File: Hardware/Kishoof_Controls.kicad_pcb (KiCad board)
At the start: 4 copper layers, 70.8 x 110 mm, 30 parts, among them J1 Conn_01x12_Pin, J10 Audio_Out_L, J11 Audio_Out_R, J12 USB_C_Receptacle, J14 Conn_01x01_Socket, J2 Conn_01x12_Pin, J3 Conn_01x12_Pin, J4 Conn_01x12_Pin, J5 WavetablePosA, J6 WavetablePosB, J7 WarpCV, J8 VOct, J9 VCA, SW1 SW_Push, SW2 Mode_Switch, SW3 Octave_Switch, SW4 ChB_Output, SW5 Encoder, U1 STF202-22T1G

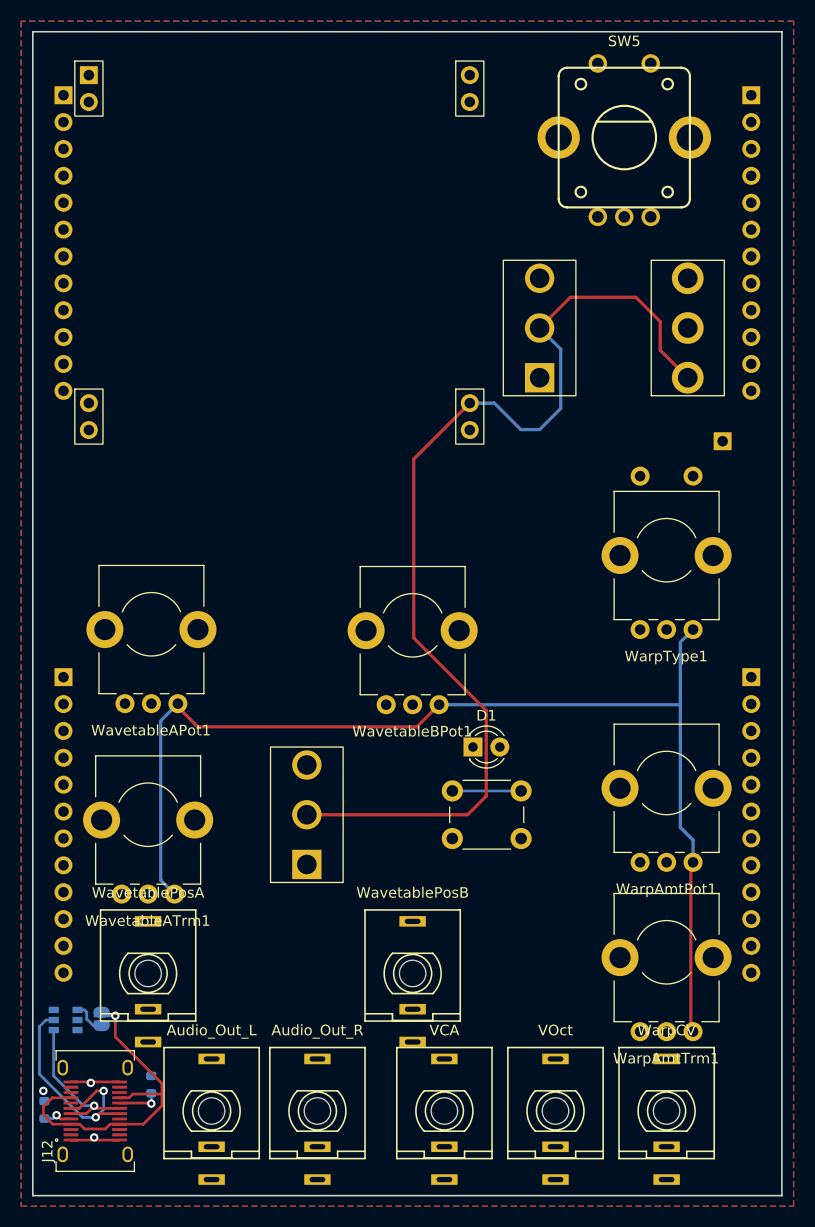
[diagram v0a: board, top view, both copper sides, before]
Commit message: Control board routed; updated lcd riser
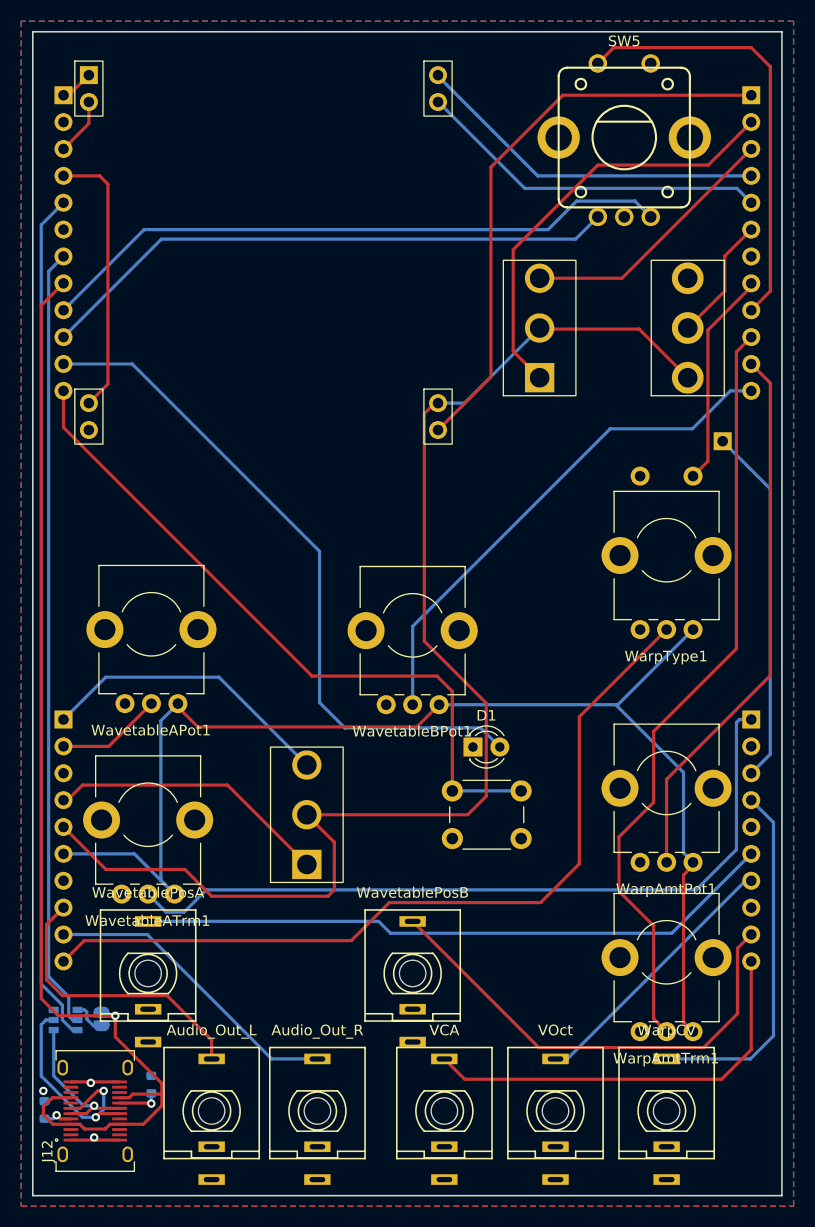
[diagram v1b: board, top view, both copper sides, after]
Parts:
- J3, J4: value Conn_01x12_Pin -> Conn_01x10_Pin; footprint Connector_PinSocket_2.54mm:PinSocket_1x12_P2.54mm_Vertical -> Connector_PinSocket_2.54mm:PinSocket_1x10_P2.54mm_Vertical
- moved J3 4.00 mm to (58.0, 104.0)
- moved J4 4.00 mm to (123.0, 104.0)
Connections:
- J1 pad 1: /LCD_SPI3_SS -> /LCD_SPI3_MOSI
- J1 pad 10: USB_VBUS -> /Encoder_Up
- J1 pad 11: /B_Octave_Btn -> /LED_Oct_B_Out
- J1 pad 12: unconnected-(J1-Pin_12-Pad12) -> /B_Octave_Btn
- J1 pad 2: /LCD_DC -> GND
- J1 pad 3: /Octave_Up -> /LCD_SPI3_SCK
- J1 pad 4: /Octave_Down -> /LCD_SPI3_SS
- J1 pad 5: unconnected-(J1-Pin_5-Pad5) -> /USB_DP
- J1 pad 6: /LCD_SPI3_MOSI -> GND
- J1 pad 7: /LCD_SPI3_SCK -> /USB_DM
- J1 pad 8: /USB_DM -> USB_VBUS
- J1 pad 9: /USB_DP -> /Encoder_Down
- J2 pad 1: unconnected-(J2-Pin_1-Pad1) -> /LCD_Backlight
- J2 pad 10: /Warp_Type_Pot -> /Warp_Amt_Trm
- J2 pad 11: /Audio_Out_R -> /Warp_Amt_Pot
- J2 pad 12: /Audio_Out_L -> /Wavetable_Pos_B_Pot
- J2 pad 2: /ChB_RM -> /Octave_Up
- J2 pad 3: /Wavetable_Pos_A_Pot -> /Octave_Down
- J2 pad 4: /Wavetable_Pos_B_CV_In -> /LCD_DC
- J2 pad 5: +3.3V -> /LCD_RESET
- J2 pad 6: GND -> Mode
- J2 pad 7: +3.3VA -> GND
- J2 pad 8: /Warp_Amt_Trm -> /Warp_Polarity_Btn
- J2 pad 9: /Warp_Amt_Pot -> /Encoder_Btn
- J3 pad 1: /LCD_RESET -> /ChB_RM
- J3 pad 10: unconnected-(J3-Pin_10-Pad10) -> /Warp_Type_Pot
- J3 pad 2: /Warp_Polarity_Btn -> /Wavetable_Pos_A_Pot
- J3 pad 3: /Encoder_Up -> GND
- J3 pad 4: /Encoder_Down -> /ChB_Mix
- J3 pad 5: /Wavetable_Pos_B_Pot -> +3.3V
- J3 pad 6: unconnected-(J3-Pin_6-Pad6) -> +3.3VA
- J3 pad 7: unconnected-(J3-Pin_7-Pad7) -> GND
- J3 pad 8: Mode -> /Audio_Out_L
- J3 pad 9: unconnected-(J3-Pin_9-Pad9) -> /Audio_Out_R
- J4 pad 1: unconnected-(J4-Pin_1-Pad1) -> /Wavetable_Pos_A_Trm
- J4 pad 10: unconnected-(J4-Pin_10-Pad10) -> /VCA_CV_In
- J4 pad 2: /LED_Oct_B_Out -> GND
- J4 pad 3: /LCD_Backlight -> /Ext_Audio_In
- J4 pad 4: /Wavetable_Pos_A_Trm -> /Warp_CV_In
- J4 pad 5: unconnected-(J4-Pin_5-Pad5) -> GND
- J4 pad 6: /ChB_Mix -> /Wavetable_Pos_A_CV_In
- J4 pad 7: unconnected-(J4-Pin_7-Pad7) -> /Pitch_CV_In
- J4 pad 8: /Encoder_Btn -> GND
- J4 pad 9: /VCA_CV_In -> /Wavetable_Pos_B_CV_In
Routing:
- net /USB_DP: track 0.00 -> 80.8 mm
- net /Warp_Type_Pot: track 0.00 -> 78.1 mm
- net USB_VBUS: track 32.3 -> 108.4 mm
- net /USB_DM: track 0.00 -> 74.1 mm
- net /Warp_Amt_Trm: track 0.00 -> 72.7 mm
- net /Wavetable_Pos_A_Trm: track 0.00 -> 72.3 mm
- net /LED_Oct_B_Out: track 0.00 -> 64.6 mm
- net /Wavetable_Pos_A_CV_In: track 0.00 -> 60.6 mm
- net /Encoder_Down: track 0.00 -> 60.4 mm
- net /B_Octave_Btn: track 6.50 -> 66.4 mm
- net /Encoder_Up: track 0.00 -> 55.2 mm
- net /LCD_Backlight: track 0.00 -> 54.3 mm
- net /Warp_Amt_Pot: track 0.00 -> 51.9 mm
- net /Wavetable_Pos_B_Pot: track 0.00 -> 48.6 mm
- net /Wavetable_Pos_B_CV_In: track 0.00 -> 45.0 mm
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- removed copper zone on In2.Cu, net (none)
- removed copper zone on In1.Cu, net GND
- removed copper zone on In2.Cu, net GND
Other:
- copper layers 4 -> 2
- board text removed: "RX"
- board text removed: "TX"

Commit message: PCBs v1.0 ordered
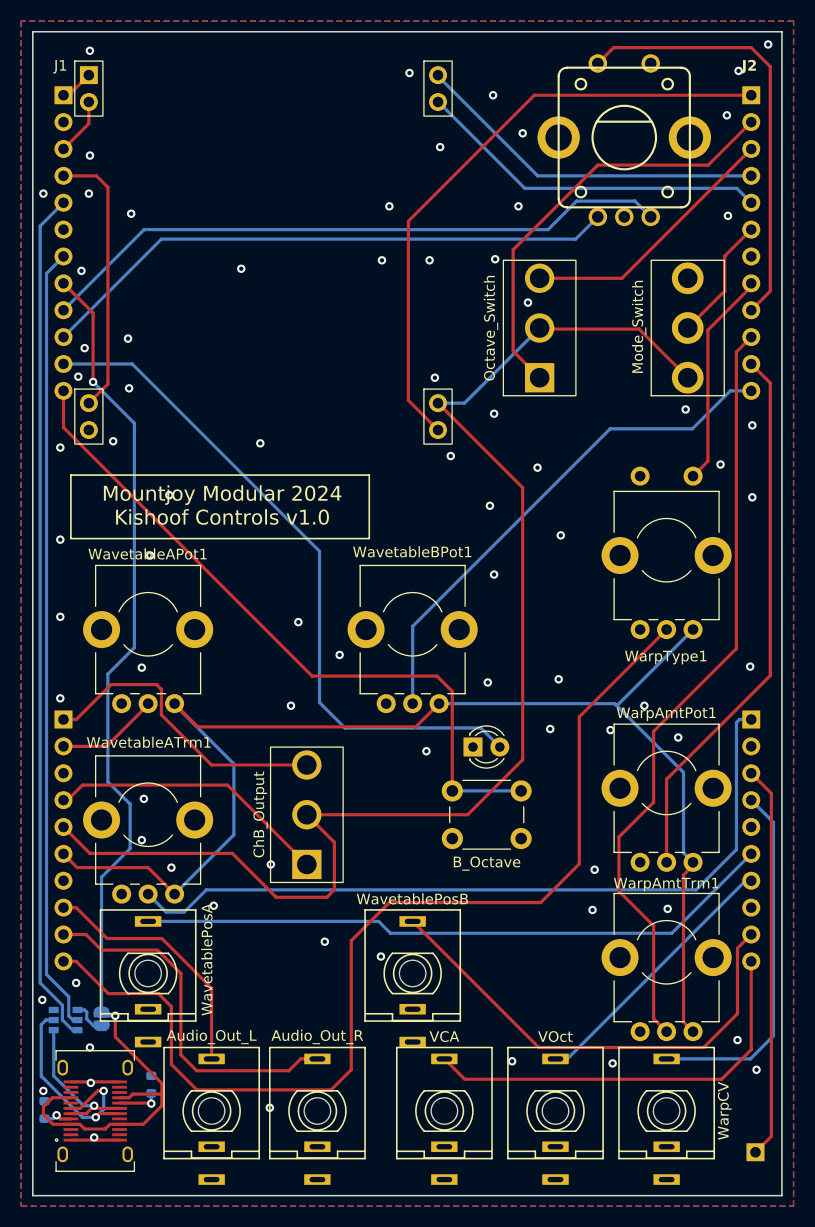
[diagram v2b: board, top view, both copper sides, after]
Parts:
- SW1: value SW_Push -> B_Octave
- moved J14 67.3 mm to (123.4, 144.9)
- moved WavetableAPot1 0.31 mm to (66.0, 95.0)
- moved WavetableBPot1 0.10 mm to (91.0, 95.0)
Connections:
- net Mode renamed /Mode
- net USB_D+ renamed /USB_D+
- net USB_D- renamed /USB_D-
- net USB_VBUS renamed /USB_VBUS
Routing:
- net /Warp_Type_Pot: track 78.1 -> 98.5 mm
- net /Audio_Out_R: track 28.9 -> 34.3 mm
- net +3.3VA: track 118.6 -> 123.5 mm
- net /LCD_Backlight: track 54.3 -> 58.2 mm
- net /Audio_Out_L: track 27.2 -> 23.8 mm
- net /Ext_Audio_In: track 34.0 -> 37.2 mm
- net +3.3V: track 123.2 -> 124.9 mm
- net /USB_VBUS: track 108.4 -> 107.0 mm, vias 1 -> 2
- net /ChB_RM: track 28.1 -> 28.9 mm
- net GND: vias 3 -> 77
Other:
- board text added: "J1"
- board text added: "J2"
- board text added: "Mountjoy Modular 2024 Kishoof Controls v1.0"
- board text removed: "GND"

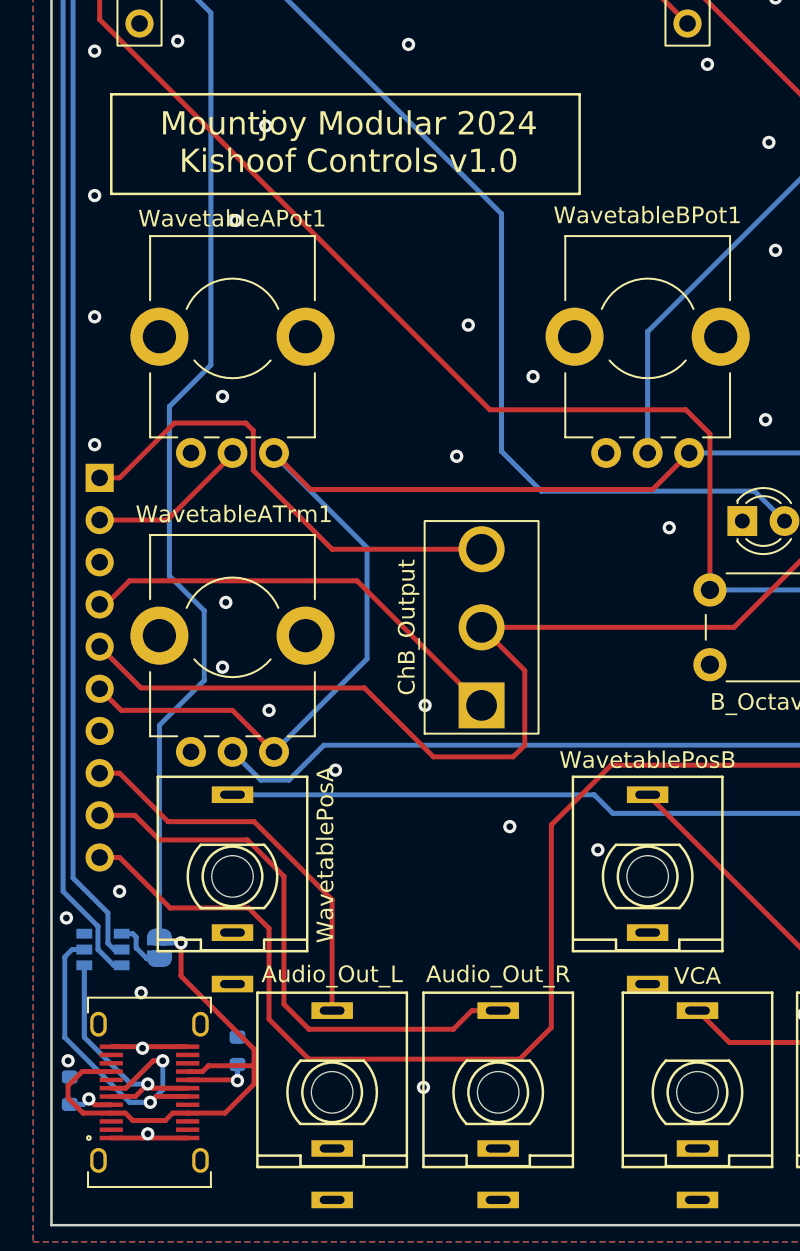
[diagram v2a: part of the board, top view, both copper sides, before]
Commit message: Updated Controls PCB to fix VCA normalisation problem
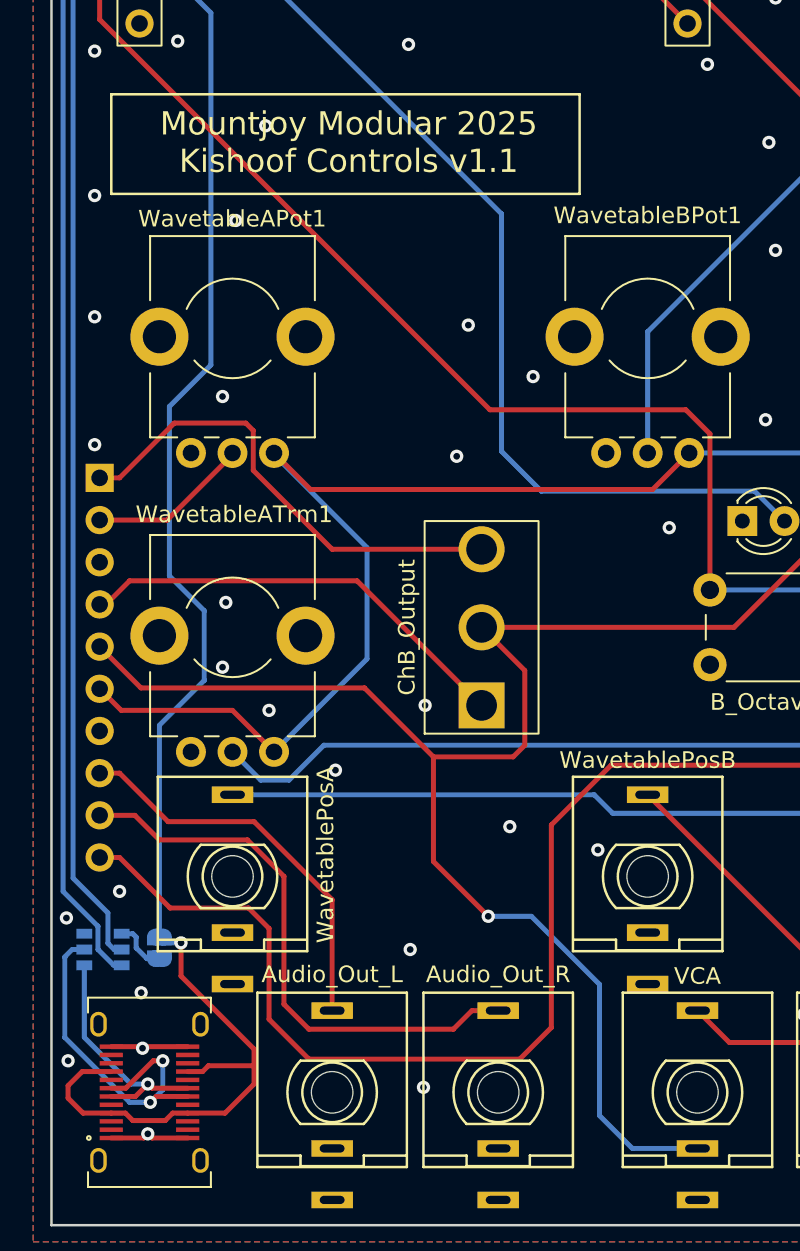
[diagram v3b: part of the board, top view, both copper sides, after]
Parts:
- removed R1, R2: 5k1, Resistor_SMD:R_0603_1608Metric
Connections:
- J12 pad A5: Net-(J12-CC1) -> unconnected-(J12-CC1-PadA5)
- J12 pad B5: Net-(J12-CC2) -> unconnected-(J12-CC2-PadB5)
- J9 pad 2: GND -> +3.3V
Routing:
- net +3.3V: track 124.9 -> 158.9 mm, vias 0 -> 1
- net Net-(J12-CC2): track 4.00 -> 0.00 mm, vias 1 -> 0
- net Net-(J12-CC1): track 2.78 -> 0.00 mm, vias 1 -> 0
- net GND: vias 77 -> 78
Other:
- board text added: "Mountjoy Modular 2025 Kishoof Controls v1.1"
- board text removed: "Mountjoy Modular 2024 Kishoof Controls v1.0"
